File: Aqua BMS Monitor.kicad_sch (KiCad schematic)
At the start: 132 parts, among them J4 Conn_01x04, J5 Conn_01x04, Q1 NMOS, Q2 PMOS, Q3 PMOS, Q4 NMOS, Q5 NMOS, Q6 NPN, Q7 NMOS, Q8 PMOS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

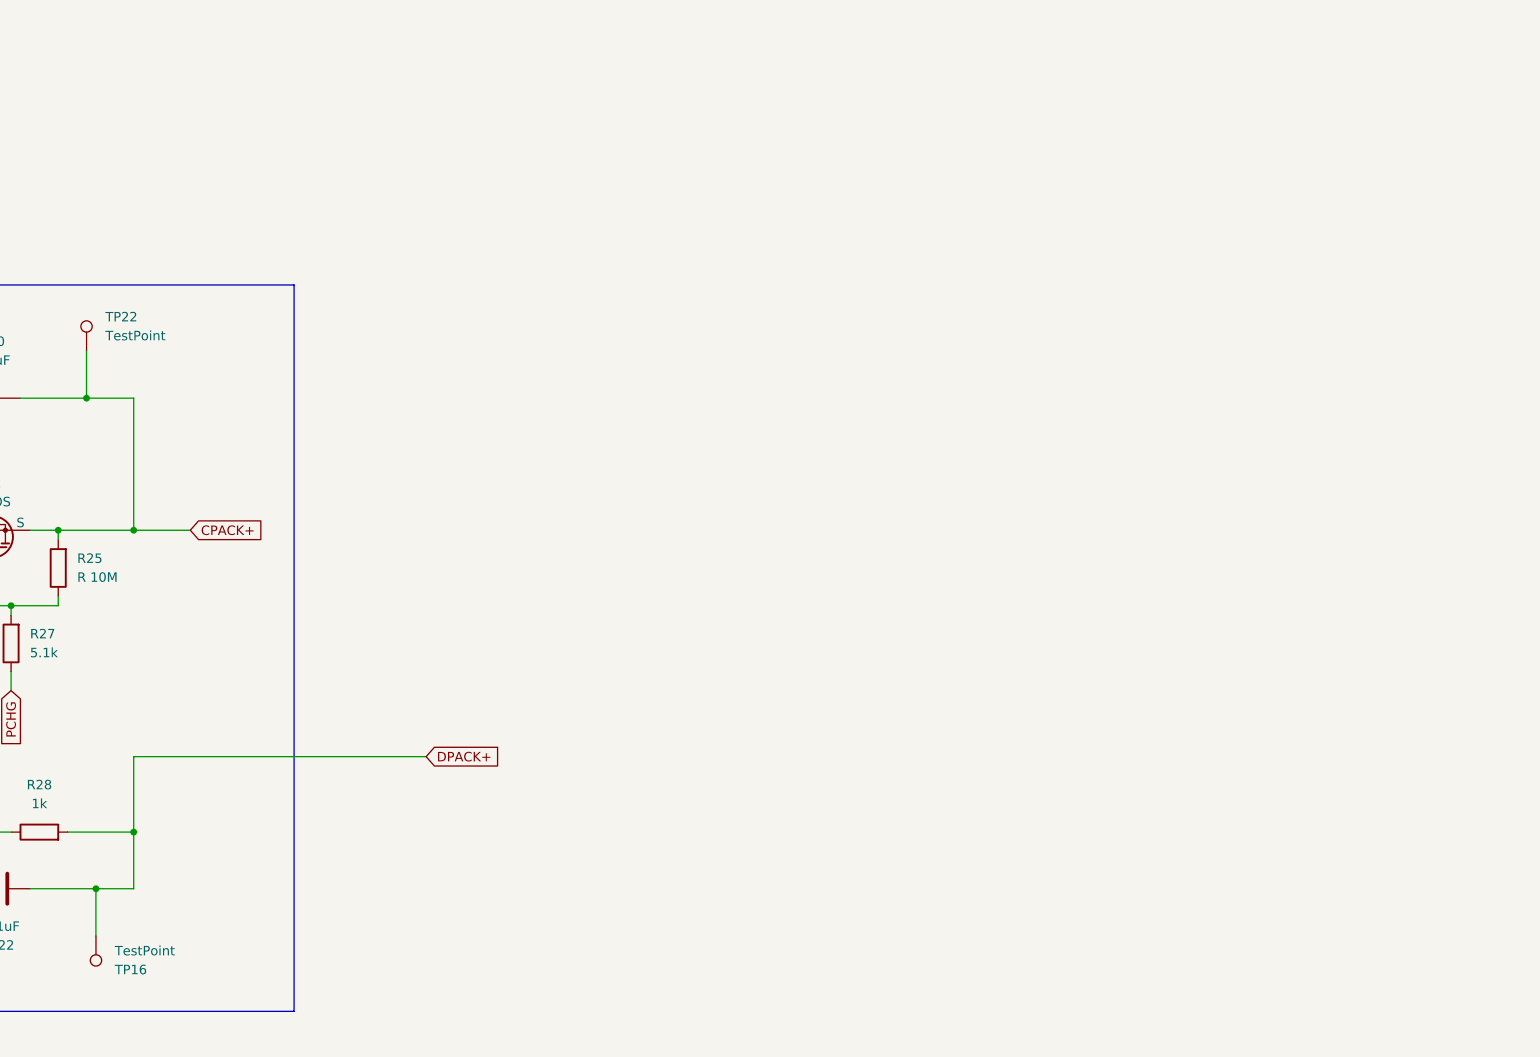
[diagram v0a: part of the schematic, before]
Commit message: Update Aqua BMS Monitor.kicad_sch
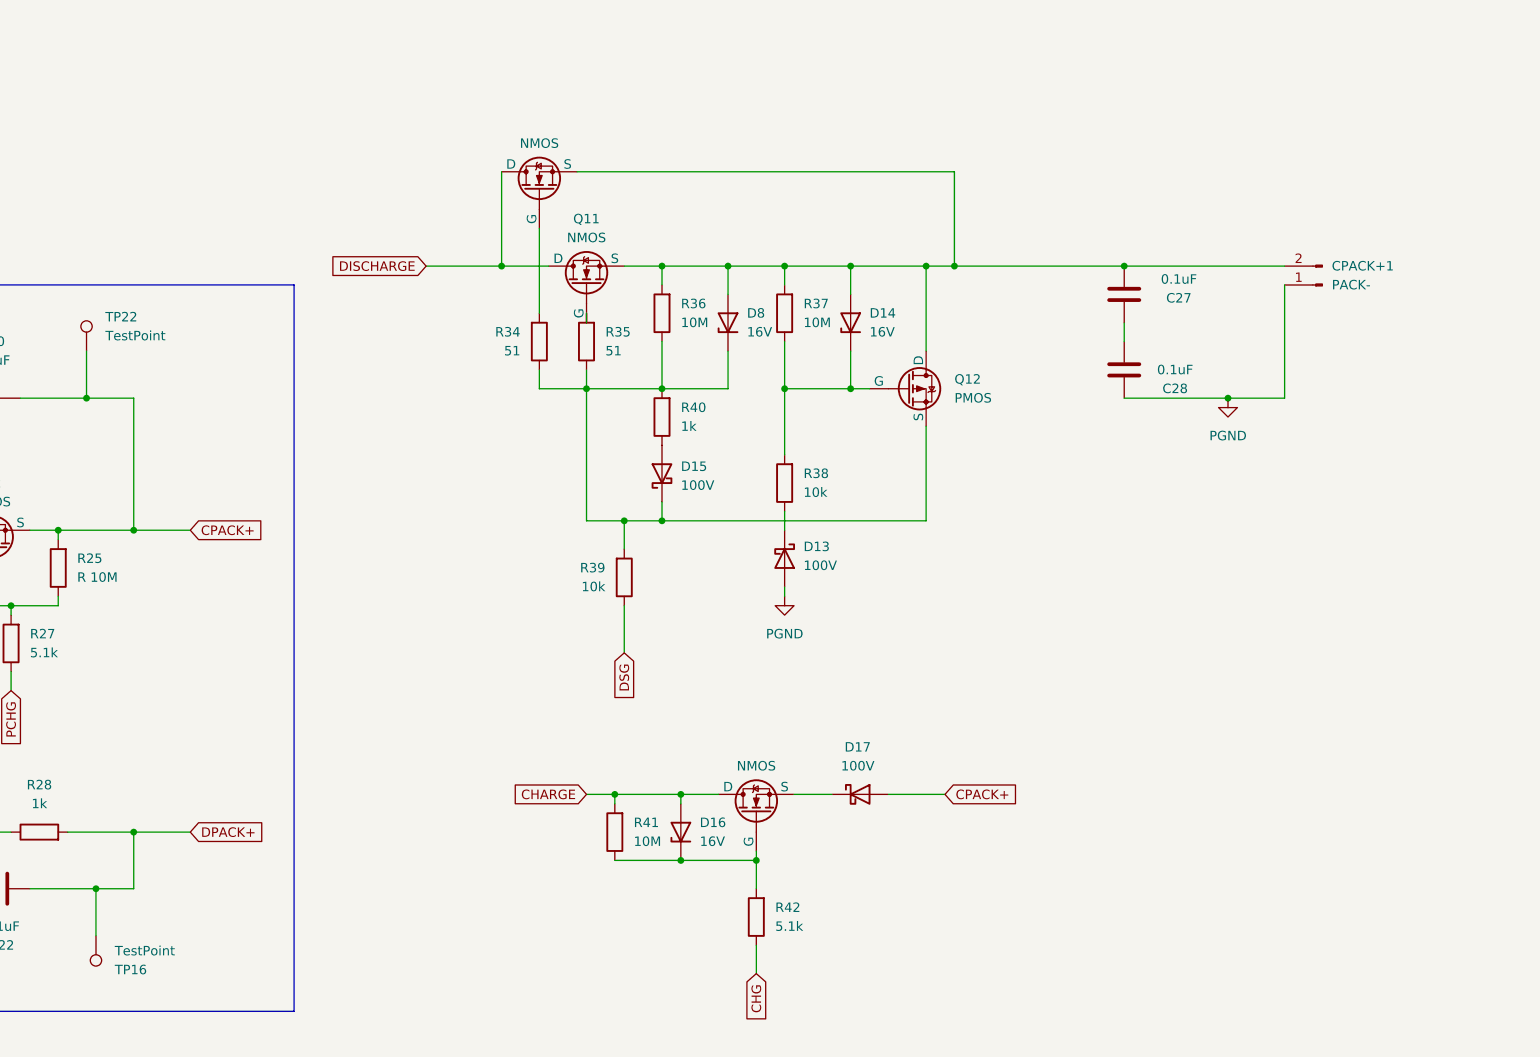
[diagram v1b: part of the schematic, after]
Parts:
- added C27, C28: 0.1uF, symbol Device:C
- added CPACK+1: PACK-, symbol Connector:Conn_01x02_Pin
- added D13, D15, D17: 100V, symbol Device:D_Schottky
- added D14, D16, D8: 16V, symbol Device:D_Zener
- added Q10, Q11, Q13: NMOS, symbol Simulation_SPICE:NMOS
- added Q12: PMOS, symbol Simulation_SPICE:PMOS
- added R34, R35: 51, symbol BQ76952PFBR:R
- added R36, R37, R41: 10M, symbol BQ76952PFBR:R
- added R38, R39: 10k, symbol BQ76952PFBR:R
- added R40: 1k, symbol BQ76952PFBR:R
- added R42: 5.1k, symbol BQ76952PFBR:R
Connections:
- net BAT+: now also D16.2 (A), Q10.1 (D), Q11.1 (D), Q13.1 (D), R41.2
- net CHG: now also R42.1
- net CPACK+: now also D17.2 (A)
- net DSG: now also R39.1
- net PGND: now also C28.2, CPACK+1.1 (Pin_1), D13.2 (A)
- new net: D13.1 (K), R38.1
- new net: Q10.2 (G), R34.2
- new net: C27.1, CPACK+1.2 (Pin_2), D14.2 (A), D8.2 (A), Q10.3 (S), Q11.3 (S), Q12.1 (D), R36.2, R37.2
- new net: D16.1 (K), Q13.2 (G), R41.1, R42.2
- new net: D15.1 (K), D8.1 (K), Q12.3 (S), R34.1, R35.1, R36.1, R39.2, R40.2
- new net: D15.2 (A), R40.1
- new net: C27.2, C28.1
- new net: D14.1 (K), Q12.2 (G), R37.1, R38.2
- new net: D17.1 (K), Q13.3 (S)
- new net: Q11.2 (G), R35.2

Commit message: Update Aqua BMS Monitor.kicad_sch
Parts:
- removed CPACK+1: PACK-, symbol Connector:Conn_01x02_Pin
- removed Q12: PMOS, symbol Simulation_SPICE:PMOS
- added 3TFuse1: ~, symbol Device:3TerminalFuse
- added C29, C32, C33: 0.1uF, symbol Device:C
- added Q14: NMOS, symbol Simulation_SPICE:NMOS
- added R43, R44: 10k, symbol BQ76952PFBR:R
- added R45: 5.1k, symbol BQ76952PFBR:R
- added R46: 20k, symbol BQ76952PFBR:R
- added RproCTL: 5.1k, symbol Device:R
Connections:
- net BAT+: now also 3TFuse1. (Out); no longer C19.1, C21.1, D16.2 (A), Q10.1 (D), Q11.1 (D), Q13.1 (D), Q3.3 (S), R26.1, R30.1, R41.2
- net CD: now also C19.1, C21.1, D16.2 (A), Q10.1 (D), Q11.1 (D), Q13.3 (S), Q3.3 (S), R26.1, R30.1, R41.2, 3TFuse1. (Out)
- net CPACK+: now also C29.1, R43.2
- net DPACK+: now also C27.1, D14.2 (A), D8.2 (A), Q10.3 (S), Q11.3 (S), R36.2, R37.2, Q14.3 (S), R44.2
- net FUSE: now also Q5.2 (G), C33.1, R45.2, R46.2, RproCTL.2; no longer Q5.1 (D), U1.38 (FUSE)
- net LD: now also R44.1
- net PACK: now also R43.1
- net PGND: now also C32.2
- net VSS: now also C33.2, R46.1
- net at D15.1 (K), D8.1 (K), R34.1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: now also Q14.1 (D)
- net at D14.1 (K), R37.1, R38.2: now also Q14.2 (G)
- net at D17.1 (K): now also Q13.1 (D); no longer Q13.3 (S)
- net at BQ296115DSGR1.8 (OUT): now also RproCTL.1; no longer Q5.2 (G)
- new net: C29.2, C32.1
- new net: R45.1, U1.38 (FUSE)
- new net: 3TFuse1. (Out), Q5.1 (D)
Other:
- note added: "Pin powering the regulator - almost certain we want it here so that it's always attached to something"
- note added: "Reason you need an NMOS for reverse protection is very interesting"
- moved on the sheet: C19, C20, C21, C22, C27, C28, D13, D14, D15, D16, D17, D8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

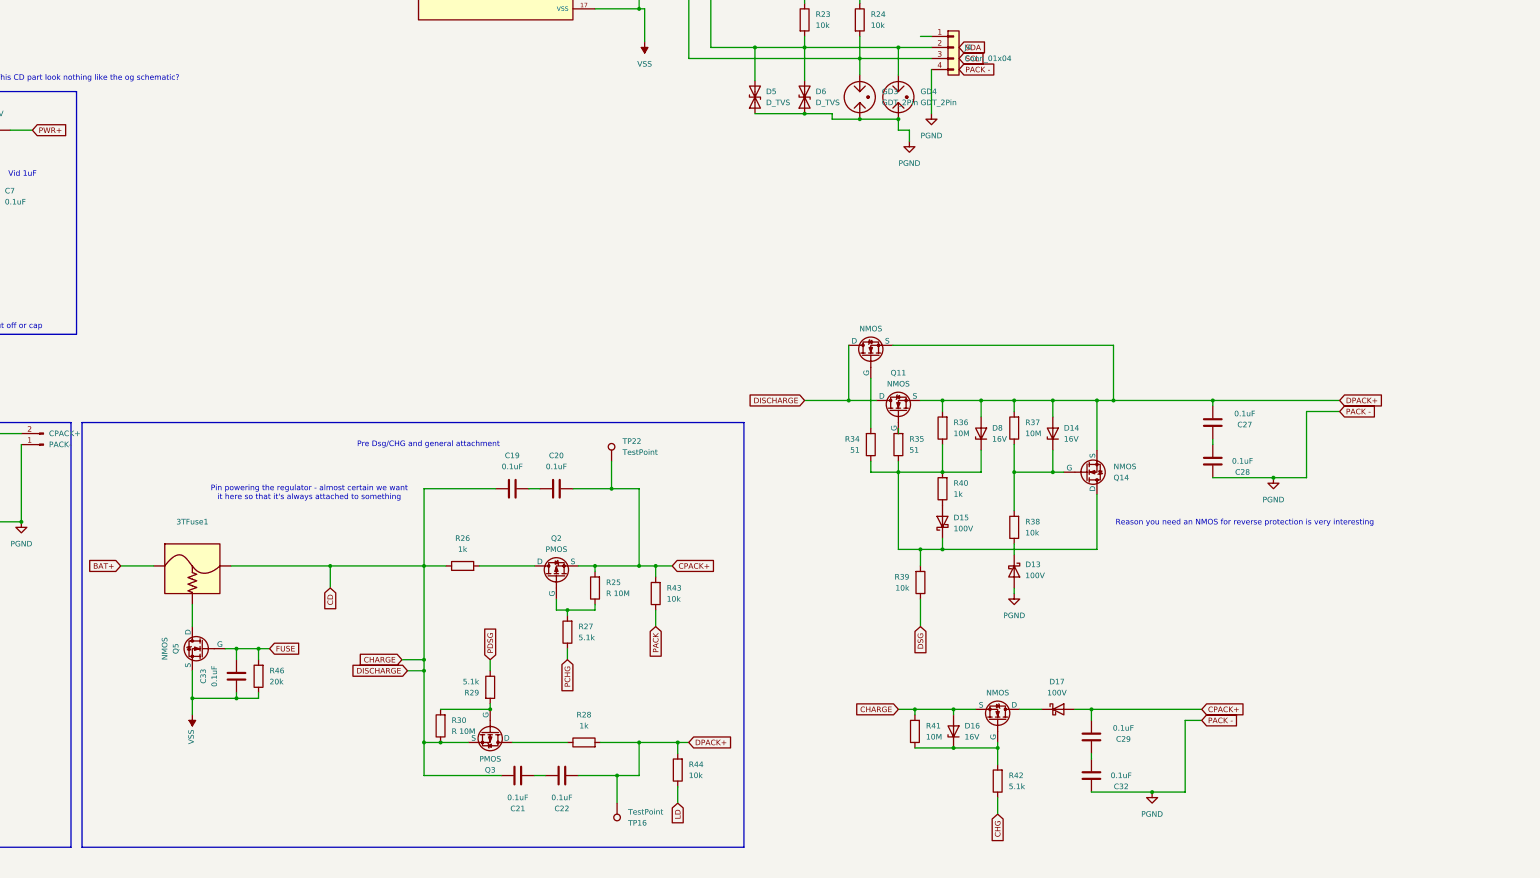
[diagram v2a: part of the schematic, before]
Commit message: Discharge/Charge Circuit v1 done
Up for review and explanation
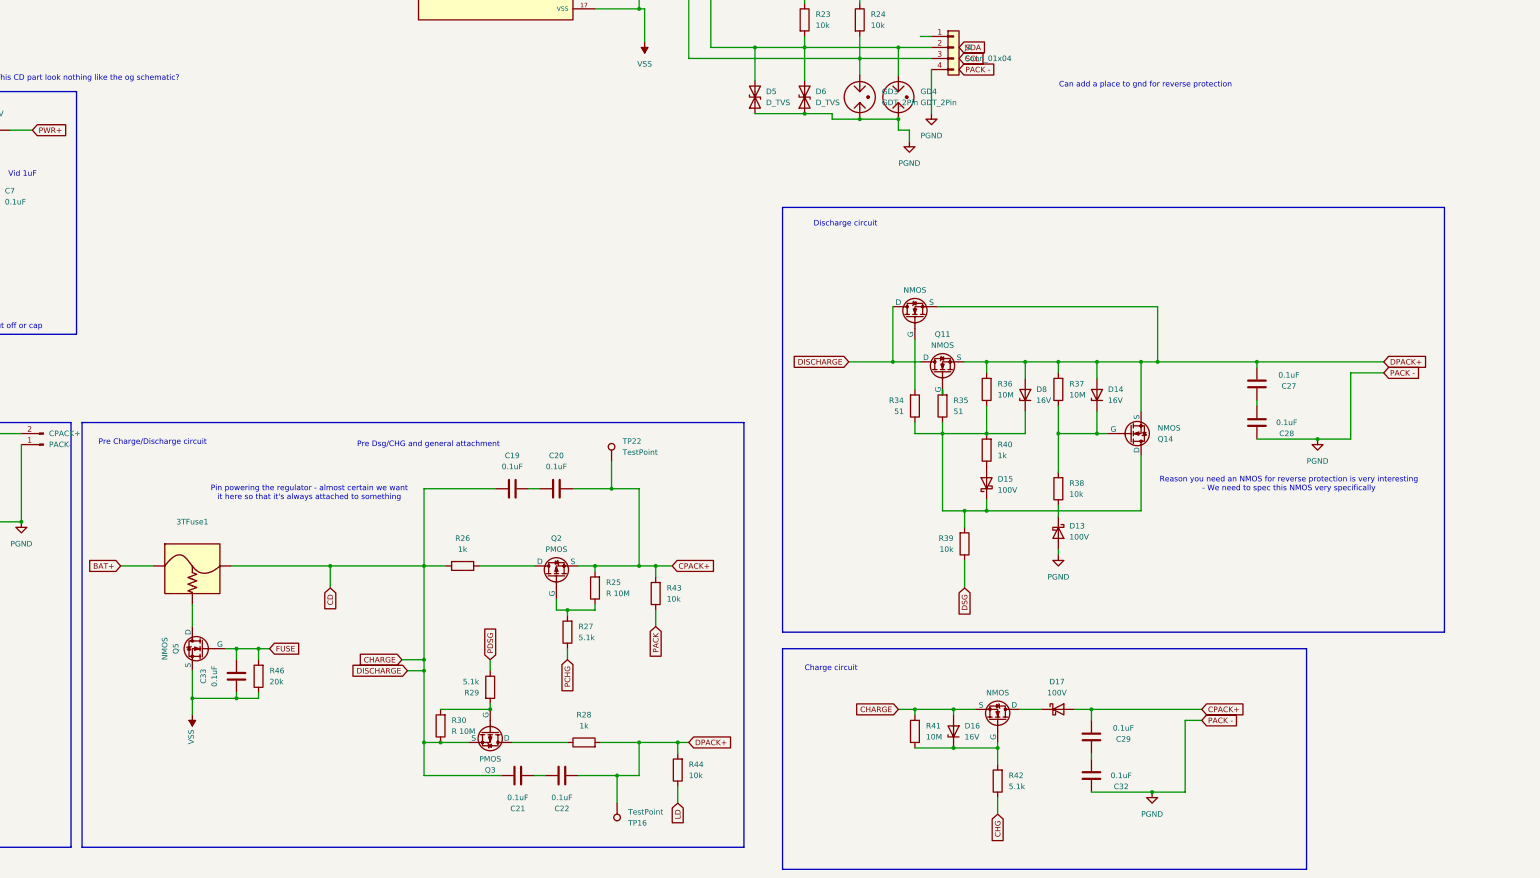
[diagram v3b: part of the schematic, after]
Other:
- note added: "Can add a place to gnd for reverse protection"
- note added: "Charge circuit"
- note added: "Discharge circuit"
- note added: "Pre Charge/Discharge circuit"
- note added: "Reason you need an NMOS for reverse protection is very interesting - We need to spec this NMOS very specifically"
- note removed: "Reason you need an NMOS for reverse protection is very interesting"
- moved on the sheet: C27, C28, D13, D14, D15, D8, Q11, Q14, R34, R35, R36, R37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

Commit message: changed size
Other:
- note added: "Blocking fets"
- moved on the sheet: R37
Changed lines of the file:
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@@
 	(generator "eeschema")
 	(generator_version "9.0")
-	(paper "A2")
+	(paper "A1")
 	(rectangle
 		(start 90.17 151.13)
@@
 	(rectangle
 		(start 368.3 342.9)
-		(end 488.95 393.7)
+		(end 476.25 393.7)
 		(stroke
 			(width 0)
@@
 		)
 	)
+	(text "Blocking fets"
+		(exclude_from_sim no)
+		(at 457.2 251.46 0)
+		(effects
+			(font
+				(size 1.27 1.27)
+			)
+		)
+	)
 	(text "Can add a place to gnd for reverse protection"
 		(exclude_from_sim no)
@@
 	)
 	(junction
-		(at 454.66 276.86)
-		(diameter 0)
-		(color 0 0 0 0)
-	)
-	(junction
 		(at 163.83 245.11)
 		(diameter 0)
@@
 	(wire
 		(pts
-			(xy 403.86 264.16) (xy 454.66 264.16)
+			(xy 403.86 264.16) (xy 450.85 264.16)
 		)
 		(stroke
@@
 	(wire
 		(pts
-			(xy 454.66 264.16) (xy 454.66 276.86)
+			(xy 450.85 264.16) (xy 450.85 276.86)
 		)
 		(stroke
@@
 	(wire
 		(pts
-			(xy 431.8 287.02) (xy 431.8 293.37)
+			(xy 431.8 288.29) (xy 431.8 293.37)
 		)
 		(stroke
@@
 	(wire
 		(pts
-			(xy 454.66 276.86) (xy 477.52 276.86)
-		)
-		(stroke
-			(width 0)
-			(type default)
-		)
-	)
-	(wire
-		(pts
 			(xy 273.05 175.26) (xy 279.4 175.26)
 		)
@@
 	(wire
 		(pts
-			(xy 450.85 276.86) (xy 454.66 276.86)
-		)
-		(stroke
-			(width 0)
-			(type default)
-		)
-	)
-	(wire
-		(pts
 			(xy 393.7 264.16) (xy 393.7 276.86)
 		)
@@
 	(wire
 		(pts
+			(xy 450.85 276.86) (xy 477.52 276.86)
+		)
+		(stroke
+			(width 0)
+			(type default)
+		)
+	)
+	(wire
+		(pts
 			(xy 556.26 160.02) (xy 558.8 160.02)
 		)
@@
 	(wire
 		(pts
-			(xy 431.8 276.86) (xy 431.8 279.4)
+			(xy 431.8 276.86) (xy 431.8 280.67)
 		)
 		(stroke
@@
 	(symbol
 		(lib_id "BQ76952PFBR:R")
-		(at 431.8 283.21 180)
+		(at 431.8 284.48 180)
 		(unit 1)
 		(exclude_from_sim no)
@@
 		(fields_autoplaced yes)
 		(property "Reference" "R37"
-			(at 434.34 281.9399 0)
+			(at 434.34 283.2099 0)
 			(effects
 				(font
@@
 		)
 		(property "Value" "10M"
-			(at 434.34 284.4799 0)
+			(at 434.34 285.7499 0)
 			(effects
 				(font
@@
 		)
 		(property "Footprint" ""
-			(at 433.578 283.21 90)
+			(at 433.578 284.48 90)
 			(effects
 				(font
@@
 		)
 		(property "Datasheet" "~"
-			(at 431.8 283.21 0)
+			(at 431.8 284.48 0)
 			(effects
 				(font
@@
 		)
 		(property "Description" "Resistor"
-			(at 431.8 283.21 0)
+			(at 431.8 284.48 0)
 			(effects
 				(font
